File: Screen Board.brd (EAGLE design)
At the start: 46.8 x 27 mm, 11 parts, among them Q1 2N2222, SW1 TL1105JAF250Q_1RBLK

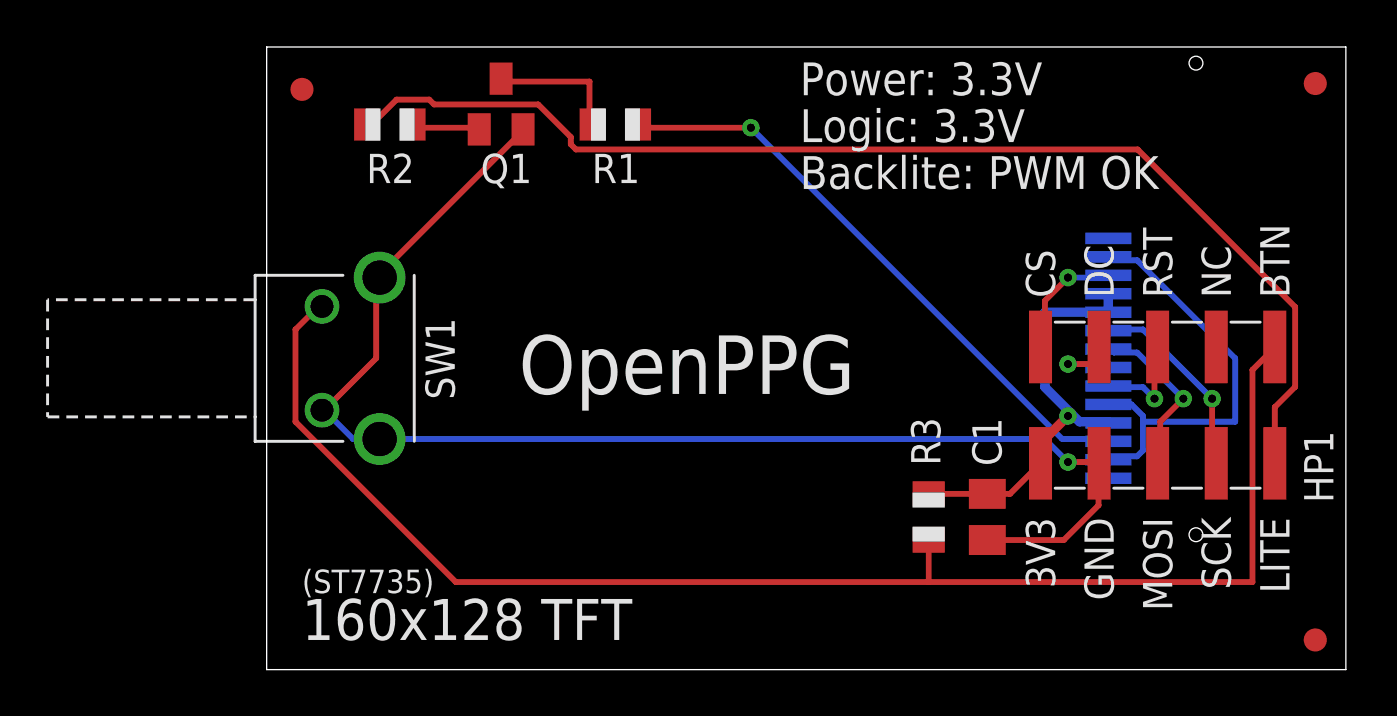
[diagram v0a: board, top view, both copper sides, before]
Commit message: Switching regulator to reduce heat, and added ground planes
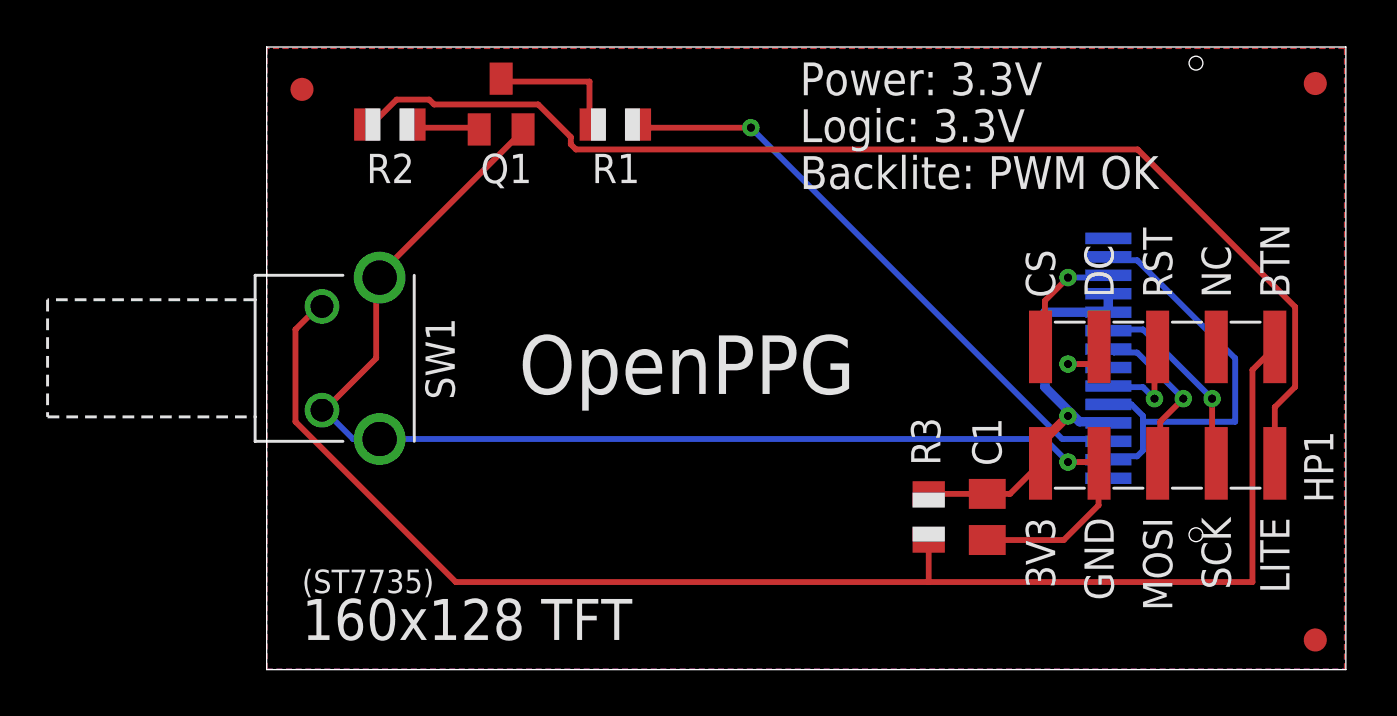
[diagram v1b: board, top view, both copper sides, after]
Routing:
- added copper zone on layer 1, net GND
- added copper zone on layer 16, net GND
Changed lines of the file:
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@@
 <?xml version="1.0" encoding="utf-8"?>
 <!DOCTYPE eagle SYSTEM "eagle.dtd">
-<eagle version="8.2.2">
+<eagle version="9.4.2">
 <drawing>
 <settings>
 <setting alwaysvectorfont="no"/>
+<setting keepoldvectorfont="yes"/>
 <setting verticaltext="up"/>
 </settings>
@@
 <param name="dpMaxLengthDifference" value="10mm"/>
 <param name="dpGapFactor" value="2.5"/>
-<param name="checkGrid" value="0"/>
 <param name="checkAngle" value="1"/>
 <param name="checkFont" value="1"/>
 <param name="checkRestrict" value="1"/>
+<param name="checkStop" value="0"/>
+<param name="checkValues" value="0"/>
+<param name="checkNames" value="1"/>
+<param name="checkWireStubs" value="1"/>
+<param name="checkPolygonWidth" value="0"/>
 <param name="useDiameter" value="13"/>
 <param name="maxErrors" value="50"/>
@@
 <attribute name="VALUE" x="29.85" y="8.62" size="1.016" layer="27" rot="R270"/>
 </element>
-<element name="U$3" library="adafruit" package="FIDUCIAL_1MM" value="FIDUCIAL" x="45.974" y="2.286"/>
-<element name="U$4" library="adafruit" package="FIDUCIAL_1MM" value="FIDUCIAL" x="45.974" y="26.416" rot="R90"/>
-<element name="U$5" library="adafruit" package="FIDUCIAL_1MM" value="FIDUCIAL" x="2.032" y="26.162"/>
-<element name="HP1" library="M20-8760546" package="M20-8760546" value="M20-8760546" x="34.059" y="8.869" locked="yes">
+<element name="U$3" library="adafruit" package="FIDUCIAL_1MM" value="FIDUCIAL" x="45.974" y="2.286" smashed="yes"/>
+<element name="U$4" library="adafruit" package="FIDUCIAL_1MM" value="FIDUCIAL" x="45.974" y="26.416" smashed="yes" rot="R90"/>
+<element name="U$5" library="adafruit" package="FIDUCIAL_1MM" value="FIDUCIAL" x="2.032" y="26.162" smashed="yes"/>
+<element name="HP1" library="M20-8760546" package="M20-8760546" value="M20-8760546" x="34.059" y="8.869" locked="yes" smashed="yes">
 <attribute name="MALE_HEADER" value="2X5" x="34.059" y="8.869" size="1.778" layer="27" display="off"/>
+<attribute name="NAME" x="46.759" y="8.234" size="1.27" layer="25" rot="R90"/>
 </element>
 <element name="SW1" library="TL1105JAF250Q_1RBLK" package="TL1105JAF250Q_1RBLK" value="TL1105JAF250Q_1RBLK" x="0" y="14.5" smashed="yes" rot="R270">
@@
 <wire x1="36.576" y1="8.128" x2="36.576" y2="9.921" width="0.254" layer="1"/>
 <wire x1="36.576" y1="9.921" x2="36.599" y2="9.944" width="0.254" layer="1"/>
+<polygon width="0.1524" layer="16">
+<vertex x="0.508" y="27.94"/>
+<vertex x="0.508" y="1.016"/>
+<vertex x="47.244" y="1.016"/>
+<vertex x="47.244" y="27.94"/>
+</polygon>
+<polygon width="0.1524" layer="1">
+<vertex x="0.508" y="1.016"/>
+<vertex x="47.244" y="1.016"/>
+<vertex x="47.244" y="27.94"/>
+<vertex x="0.508" y="27.94"/>
+</polygon>
 </signal>
 <signal name="SCK">
@@
 </signal>
 </signals>
+<mfgpreviewcolors>
+<mfgpreviewcolor name="soldermaskcolor" color="0xC8008000"/>
+<mfgpreviewcolor name="silkscreencolor" color="0xFFFEFEFE"/>
+<mfgpreviewcolor name="backgroundcolor" color="0xFF282828"/>
+<mfgpreviewcolor name="coppercolor" color="0xFFFFBF00"/>
+<mfgpreviewcolor name="substratecolor" color="0xFF786E46"/>
+</mfgpreviewcolors>
 </board>
 </drawing>
